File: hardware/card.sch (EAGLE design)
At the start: 91 parts, among them J1 UE27AC54100, J2 MICROSD, J3 0541323062, J4 6-PIN_2MM-V, J5 JST_2PIN, J6 B2PS-VH(LF)(SN), J7 MINI-USB-UX60A-MB-5ST, J8 JST_2PIN, U1 ATSAMD21J_QFN, U2 TS3USB221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

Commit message: fix a cap with the wrong footprint
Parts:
- C7: device rcl:C-USC0805 -> card:C-USC0603
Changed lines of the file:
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@@
 <part name="SUPPLY64" library="supply2" library_urn="urn:adsk.eagle:library:372" deviceset="GND" device=""/>
 <part name="SUPPLY58" library="supply2" library_urn="urn:adsk.eagle:library:372" deviceset="GND" device=""/>
-<part name="C7" library="rcl" library_urn="urn:adsk.eagle:library:334" deviceset="C-US" device="C0805" package3d_urn="urn:adsk.eagle:package:23617/2" value="10uF"/>
+<part name="C7" library="card" deviceset="C-US" device="C0603" value="10uF"/>
 <part name="U5" library="lib-card" deviceset="TLV70233" device="DBVR"/>
 <part name="SUPPLY56" library="RoboJackets-Supplies" deviceset="VBATT" device=""/>

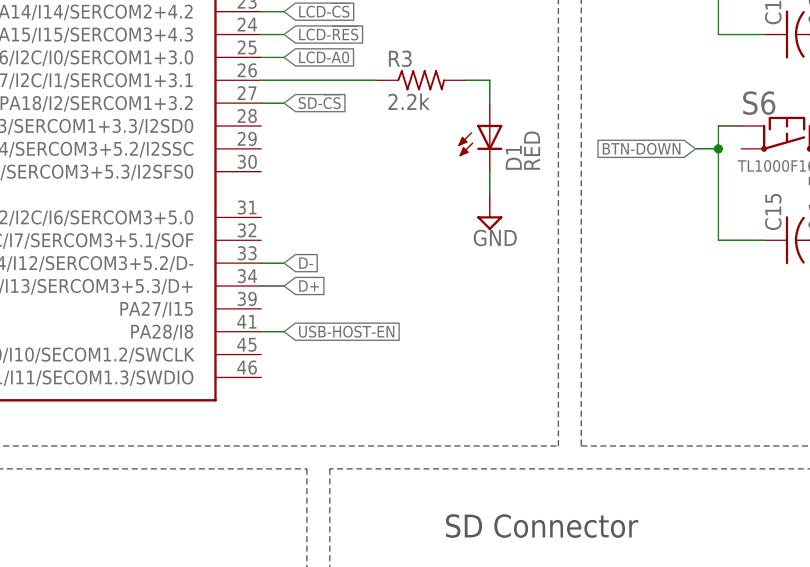
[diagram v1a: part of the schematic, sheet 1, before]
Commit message: exported gerbers
swapped the power switch connector
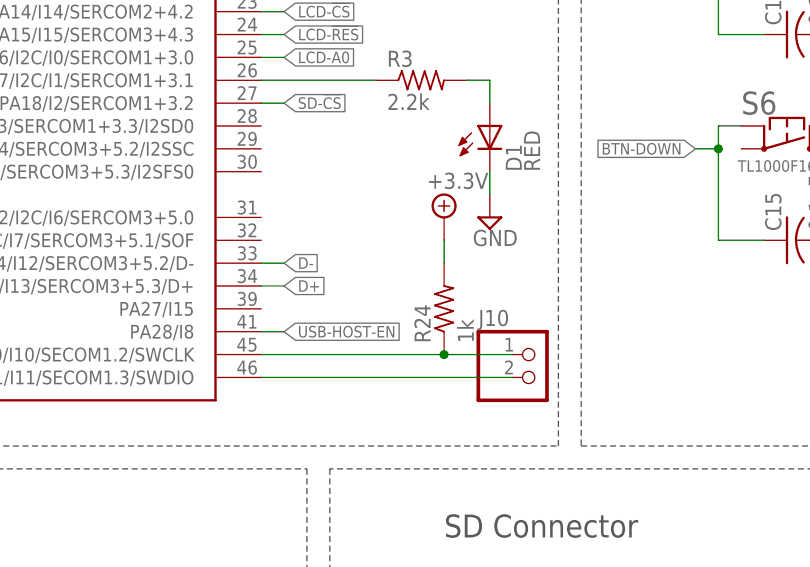
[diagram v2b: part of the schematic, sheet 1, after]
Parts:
- added J10: (no value), RoboJackets-Connectors:CONN-2VERT
- added R24: 1k, rcl:R-US_R0603
- J6: value B2PS-VH(LF)(SN) -> JST_2PIN; device RoboJackets-Connectors:B2PS-VH(LF)(SN) -> CardReader:JST_2PIN
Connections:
- new net SWCLK: J10.1, R24.1, U1.PA30/I10/SECOM1.2/SWCLK
- new net SWDIO: J10.2, U1.PA31/I11/SECOM1.3/SWDIO
- net +3.3V: now also R24.2
- net BATT: now also J6.1; no longer J6.2
- net VBATT: now also J6.2; no longer J6.1
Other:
- moved on the sheet: J6
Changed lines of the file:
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@@
 <part name="R7" library="rcl" library_urn="urn:adsk.eagle:library:334" deviceset="R-US_" device="R0603" package3d_urn="urn:adsk.eagle:package:23555/2" value="1k"/>
 <part name="SUPPLY40" library="lib-card" deviceset="+3.3V" device=""/>
-<part name="J6" library="RoboJackets-Connectors" deviceset="B2P?-VH(LF)(SN)" device="S"/>
+<part name="J6" library="CardReader" deviceset="JST_2PIN" device=""/>
 <part name="R21" library="rcl" library_urn="urn:adsk.eagle:library:334" deviceset="R-US_" device="R0603" package3d_urn="urn:adsk.eagle:package:23555/2" value="0"/>
 <part name="C24" library="rcl" library_urn="urn:adsk.eagle:library:334" deviceset="C-US" device="C0603" package3d_urn="urn:adsk.eagle:package:23616/2" value="1uF"/>
@@
 <part name="D10" library="RoboJackets-LEDs" deviceset="LED-SMD" device="" technology="-YELLOW" value="YELLOW"/>
 <part name="D11" library="RoboJackets-LEDs" deviceset="LED-SMD" device="" technology="-RED" value="RED"/>
+<part name="R24" library="rcl" library_urn="urn:adsk.eagle:library:334" deviceset="R-US_" device="R0603" package3d_urn="urn:adsk.eagle:package:23555/2" value="1k"/>
+<part name="SUPPLY68" library="lib-card" deviceset="+3.3V" device=""/>
+<part name="J10" library="RoboJackets-Connectors" deviceset="CONN-2" device="VERT"/>
 </parts>
 <sheets>
@@
 <instance part="D3" gate="G$1" x="251.46" y="144.78"/>
 <instance part="D1" gate="G$1" x="132.08" y="119.38" rot="R90"/>
+<instance part="R24" gate="G$1" x="127" y="101.6" rot="R90"/>
+<instance part="SUPPLY68" gate="P" x="127" y="111.76"/>
+<instance part="J10" gate="G$1" x="137.16" y="93.98"/>
 </instances>
 <busses>
@@
 <wire x1="200.66" y1="114.3" x2="203.2" y2="114.3" width="0.1524" layer="91"/>
 </segment>
+<segment>
+<pinref part="SUPPLY68" gate="P" pin="+3.3V"/>
+<pinref part="R24" gate="G$1" pin="2"/>
+<wire x1="127" y1="109.22" x2="127" y2="106.68" width="0.1524" layer="91"/>
+</segment>
 </net>
 <net name="SD-!CS" class="0">
@@
 <wire x1="246.38" y1="154.94" x2="248.92" y2="154.94" width="0.1524" layer="91"/>
 <pinref part="D2" gate="G$1" pin="K"/>
+</segment>
+</net>
+<net name="SWCLK" class="0">
+<segment>
+<pinref part="U1" gate="G$1" pin="PA30/I10/SECOM1.2/SWCLK"/>
+<wire x1="106.68" y1="96.52" x2="127" y2="96.52" width="0.1524" layer="91"/>
+<pinref part="R24" gate="G$1" pin="1"/>
+<wire x1="127" y1="96.52" x2="134.62" y2="96.52" width="0.1524" layer="91"/>
+<junction x="127" y="96.52"/>
+<pinref part="J10" gate="G$1" pin="1"/>
+</segment>
+</net>
+<net name="SWDIO" class="0">
+<segment>
+<pinref part="U1" gate="G$1" pin="PA31/I11/SECOM1.3/SWDIO"/>
+<wire x1="106.68" y1="93.98" x2="134.62" y2="93.98" width="0.1524" layer="91"/>
+<pinref part="J10" gate="G$1" pin="2"/>
 </segment>
 </net>
@@
 <instance part="R16" gate="G$1" x="160.02" y="167.64" rot="R270"/>
 <instance part="SUPPLY51" gate="GND" x="160.02" y="160.02"/>
-<instance part="J6" gate="G$1" x="233.68" y="109.22" smashed="yes">
-<attribute name="NAME" x="228.6" y="116.84" size="1.778" layer="95" font="vector" align="top-left"/>
+<instance part="J6" gate="G$1" x="233.68" y="106.68" smashed="yes" rot="R180">
+<attribute name="NAME" x="238.76" y="99.06" size="1.778" layer="95" font="vector" rot="R180" align="top-left"/>
 </instance>
 <instance part="R21" gate="G$1" x="246.38" y="106.68" rot="R90"/>
@@
 </segment>
 <segment>
-<pinref part="J6" gate="G$1" pin="1"/>
-<wire x1="238.76" y1="111.76" x2="241.3" y2="111.76" width="0.1524" layer="91"/>
 <pinref part="SUPPLY61" gate="G$1" pin="VBATT"/>
 <wire x1="241.3" y1="111.76" x2="241.3" y2="114.3" width="0.1524" layer="91"/>
 <pinref part="R21" gate="G$1" pin="2"/>
 <wire x1="246.38" y1="111.76" x2="241.3" y2="111.76" width="0.1524" layer="91"/>
+<wire x1="241.3" y1="111.76" x2="241.3" y2="109.22" width="0.1524" layer="91"/>
 <junction x="241.3" y="111.76"/>
+<pinref part="J6" gate="G$1" pin="2"/>
+<wire x1="241.3" y1="109.22" x2="238.76" y2="109.22" width="0.1524" layer="91"/>
 </segment>
 <segment>
@@
 <wire x1="241.3" y1="86.36" x2="241.3" y2="99.06" width="0.1524" layer="91"/>
 <junction x="241.3" y="86.36"/>
-<pinref part="J6" gate="G$1" pin="2"/>
 <wire x1="241.3" y1="99.06" x2="241.3" y2="101.6" width="0.1524" layer="91"/>
 <wire x1="241.3" y1="101.6" x2="241.3" y2="106.68" width="0.1524" layer="91"/>
-<wire x1="241.3" y1="106.68" x2="238.76" y2="106.68" width="0.1524" layer="91"/>
 <label x="238.76" y="101.6" size="1.27" layer="95" rot="R180" xref="yes"/>
 <wire x1="238.76" y1="101.6" x2="241.3" y2="101.6" width="0.1524" layer="91"/>
@@
 <pinref part="C32" gate="G$1" pin="2"/>
 <wire x1="246.38" y1="99.06" x2="246.38" y2="96.52" width="0.1524" layer="91"/>
-</segment>
-<segment>
+<pinref part="J6" gate="G$1" pin="1"/>
+<wire x1="241.3" y1="106.68" x2="238.76" y2="106.68" width="0.1524" layer="91"/>
+</segment>
+<segment>

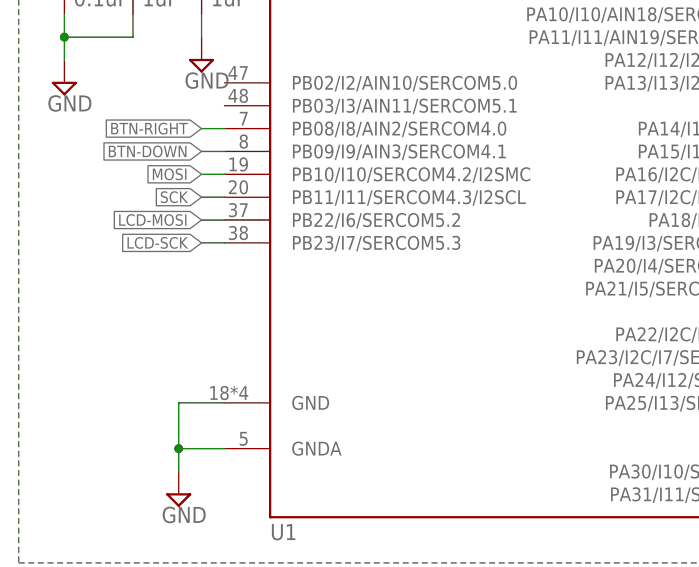
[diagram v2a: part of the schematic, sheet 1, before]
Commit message: fix positioning of display and mounting holes on case top and bottom
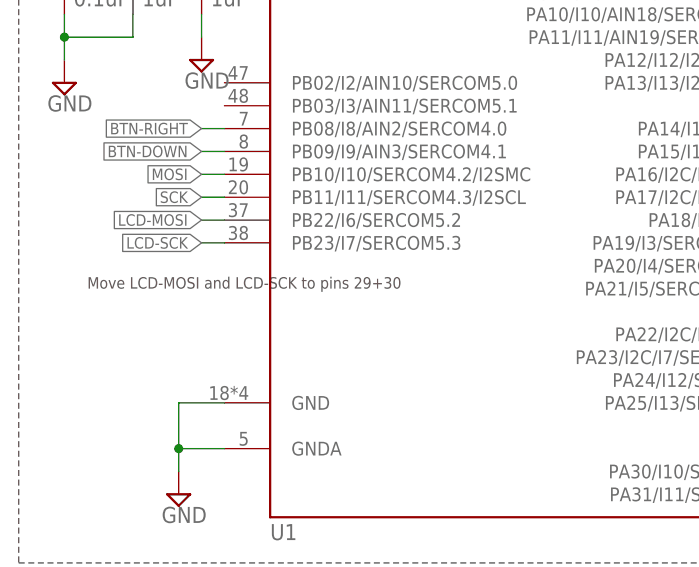
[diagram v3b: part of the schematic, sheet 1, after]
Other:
- note added: "Move LCD-MOSI and LCD-SCK to pins 29+30"
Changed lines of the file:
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@@
 <text x="182.88" y="127" size="2.54" layer="97">LCD Display</text>
 <text x="193.04" y="104.14" size="1.27" layer="97">LCD Backlight</text>
+<text x="15.24" y="116.84" size="1.27" layer="97">Move LCD-MOSI and LCD-SCK to pins 29+30</text>
 </plain>
 <instances>
